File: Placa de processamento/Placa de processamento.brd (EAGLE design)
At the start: 90.2 x 100 mm, 9 parts

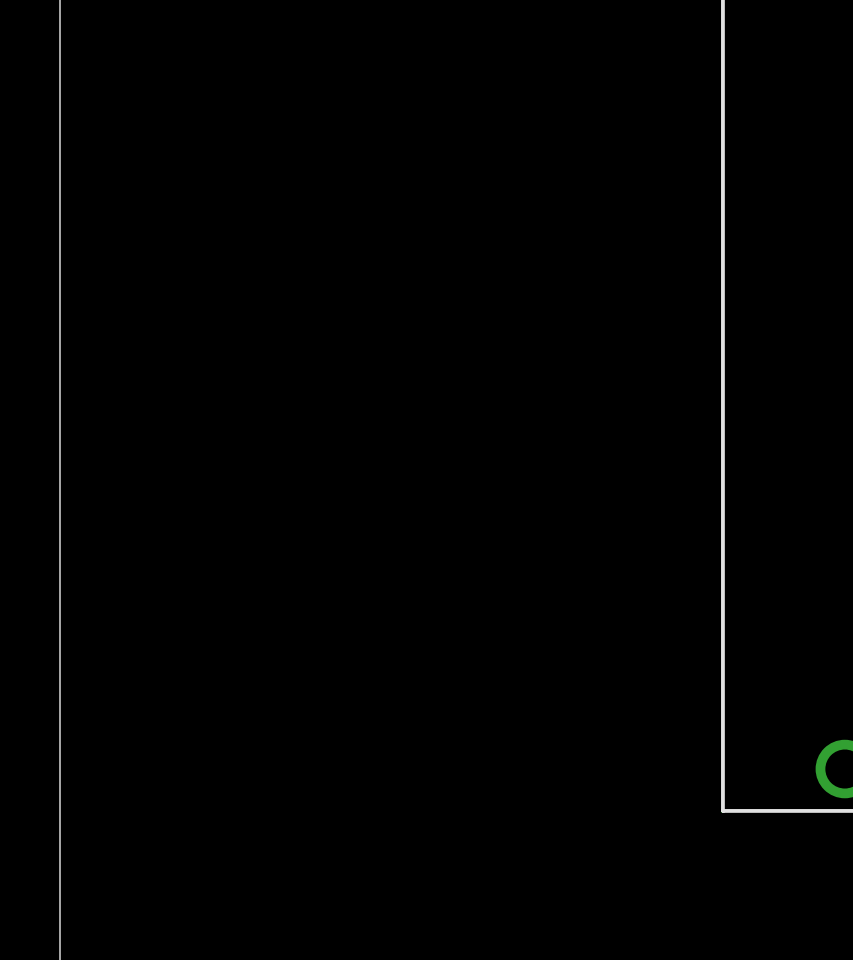
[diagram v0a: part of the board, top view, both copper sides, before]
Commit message: Conexões em placa de processamento
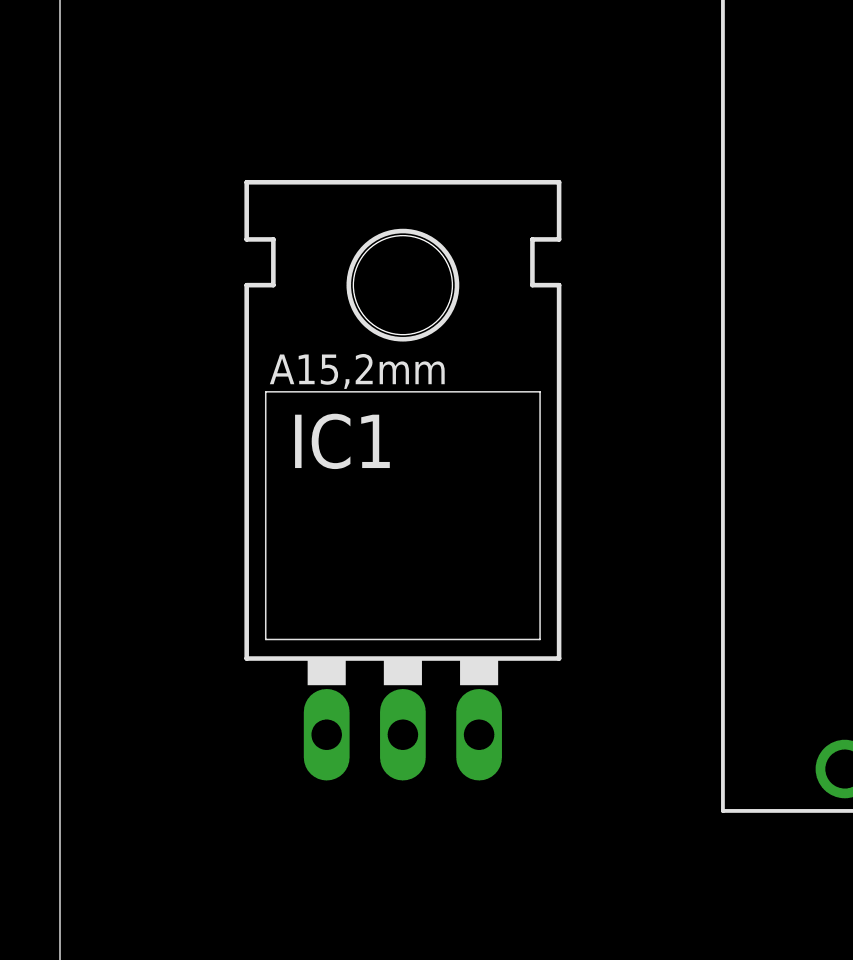
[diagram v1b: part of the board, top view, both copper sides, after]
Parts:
- added IC1: (no value), v-reg:78XXL
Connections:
- new net 3V3: U$2.3V3, U$5.2, U$7.VCC, U$9.1
- new net 5V: IC1.OUT, U$8.VCC
- new net BUZZER: U$5.1, U$9.26
- new net CS: U$2.CS, U$9.8
- new net GND: IC1.GND, U$2.GND, U$3.2, U$7.GND, U$8.GND, U$9.2, U$9.29
- new net M0: U$8.M0, U$9.21
- new net M1: U$8.M1, U$9.22
- new net MISO: U$2.MISO, U$9.10
- new net MOSI: U$2.MOSI, U$9.15
- new net N$3: U$8.AUX
- new net N$5: U$1.PR1
- new net N$6: U$1.PL1
- new net OPTOACOPLADOR1: U$6.1, U$9.19
- new net OPTOACOPLADOR2: U$6.2, U$9.20
- new net RX1: U$7.TX, U$9.3
- new net RX2: U$8.TXD, U$9.6
- new net SCLK: U$2.CLK, U$9.9
- new net SKIB1: U$4.1, U$9.28
- new net SKIB2: U$4.2, U$9.27
- new net TX1: U$7.RX, U$9.5
- new net TX2: U$8.RXD, U$9.7
- new net VIN: IC1.IN, U$1.PL3, U$1.PR3, U$9.30
- new net V_BATTERY: U$1.PL2, U$1.PR2, U$3.1
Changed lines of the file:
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@@
 </layers>
 <board>
-<fusionsync huburn="a.YnVzaW5lc3M6ZGlzY2VudGUxNzg" projecturn="a.YnVzaW5lc3M6ZGlzY2VudGUxNzgjRDIwMjIwNjExNTMyNjQzNTAx" f3durn="urn:adsk.wipprod:dm.lineage:LO0rVtrmTNmc-QnwxbZBTA" pcbguid="9d58484e-0a02-4060-8550-79589bd949fc" lastpulledtime="" lastsyncedchangeguid="" latestrevisionid="46605ec0-6288-40dc-83f6-c90f963cb555" lastsyncedrevisionid="46605ec0-6288-40dc-83f6-c90f963cb555" lastboardhashguid="0044dba3-1b92-d3f1-3d10-6736c9c82925" lastpushedtime="2024-04-18T17:53:33Z" linktopcb3d="true"/>
+<fusionsync huburn="a.YnVzaW5lc3M6ZGlzY2VudGUxNzg" projecturn="a.YnVzaW5lc3M6ZGlzY2VudGUxNzgjRDIwMjIwNjExNTMyNjQzNTAx" f3durn="urn:adsk.wipprod:dm.lineage:LO0rVtrmTNmc-QnwxbZBTA" pcbguid="" lastpulledtime="" lastsyncedchangeguid="" latestrevisionid="46605ec0-6288-40dc-83f6-c90f963cb555" lastsyncedrevisionid="46605ec0-6288-40dc-83f6-c90f963cb555" lastboardhashguid="0044dba3-1b92-d3f1-3d10-6736c9c82925" lastpushedtime="2024-04-18T17:53:33Z" linktopcb3d="true"/>
 <plain>
 <wire x1="0" y1="0" x2="90.15" y2="0" width="0" layer="20"/>
@@
 <attribute name="NAME" x="52.07" y="12.7" size="1.27" layer="21" rot="R90"/>
 </element>
+<element name="IC1" library="v-reg" library_urn="urn:adsk.eagle:library:409" package="78XXL" package3d_urn="urn:adsk.eagle:package:30361/1" value="" x="11.43" y="39.37" smashed="yes">
+<attribute name="NAME" x="7.62" y="44.45" size="1.778" layer="25" ratio="10"/>
+<attribute name="POPULARITY" value="10" x="11.43" y="39.37" size="1.778" layer="27" display="off"/>
+<attribute name="VALUE" x="7.493" y="41.91" size="1.778" layer="27" ratio="10"/>
+</element>
 </elements>
 <signals>
+<signal name="3V3">
+<contactref element="U$9" pad="1"/>
+<contactref element="U$7" pad="VCC"/>
+<contactref element="U$2" pad="3V3"/>
+<contactref element="U$5" pad="2"/>
+<wire x1="17.78" y1="91.44" x2="60.071" y2="78.74" width="0" layer="19" extent="1-1"/>
+<wire x1="79.58" y1="13.96" x2="60.071" y2="78.74" width="0" layer="19" extent="1-1"/>
+<wire x1="6.35" y1="11.63" x2="79.58" y2="13.96" width="0" layer="19" extent="1-1"/>
+</signal>
+<signal name="GND">
+<contactref element="U$9" pad="2"/>
+<contactref element="U$9" pad="29"/>
+<contactref element="U$7" pad="GND"/>
+<contactref element="U$2" pad="GND"/>
+<contactref element="U$8" pad="GND"/>
+<contactref element="U$3" pad="2"/>
+<contactref element="IC1" pad="GND"/>
+<wire x1="41.402" y1="34.417" x2="60.071" y2="66.04" width="0" layer="19" extent="1-1"/>
+<wire x1="54.81" y1="16.5" x2="41.402" y2="34.417" width="0" layer="19" extent="1-1"/>
+<wire x1="79.58" y1="16.5" x2="54.81" y2="16.5" width="0" layer="19" extent="1-1"/>
+<wire x1="6.35" y1="19.25" x2="41.402" y2="34.417" width="0" layer="19" extent="1-1"/>
+<wire x1="11.43" y1="35.56" x2="6.35" y2="19.25" width="0" layer="19" extent="1-1"/>
+<wire x1="7.62" y1="91.44" x2="60.071" y2="66.04" width="0" layer="19" extent="1-1"/>
+</signal>
+<signal name="TX1">
+<contactref element="U$9" pad="5"/>
+<contactref element="U$7" pad="RX"/>
+<wire x1="6.35" y1="14.17" x2="79.58" y2="24.12" width="0" layer="19" extent="1-1"/>
+</signal>
+<signal name="RX1">
+<contactref element="U$9" pad="3"/>
+<contactref element="U$7" pad="TX"/>
+<wire x1="6.35" y1="16.71" x2="79.58" y2="19.04" width="0" layer="19" extent="1-1"/>
+</signal>
+<signal name="MISO">
+<contactref element="U$9" pad="10"/>
+<contactref element="U$2" pad="MISO"/>
+<wire x1="79.58" y1="36.82" x2="60.071" y2="68.58" width="0" layer="19" extent="1-1"/>
+</signal>
+<signal name="MOSI">
+<contactref element="U$9" pad="15"/>
+<contactref element="U$2" pad="MOSI"/>
+<wire x1="79.58" y1="49.52" x2="60.071" y2="73.66" width="0" layer="19" extent="1-1"/>
+</signal>
+<signal name="SCLK">
+<contactref element="U$9" pad="9"/>
+<contactref element="U$2" pad="CLK"/>
+<wire x1="79.58" y1="34.28" x2="60.071" y2="71.12" width="0" layer="19" extent="1-1"/>
+</signal>
+<signal name="CS">
+<contactref element="U$9" pad="8"/>
+<contactref element="U$2" pad="CS"/>
+<wire x1="79.58" y1="31.74" x2="60.071" y2="76.2" width="0" layer="19" extent="1-1"/>
+</signal>
+<signal name="M0">
+<contactref element="U$9" pad="21"/>
+<contactref element="U$8" pad="M0"/>
+<wire x1="26.162" y1="34.417" x2="54.81" y2="36.82" width="0" layer="19" extent="1-1"/>
+</signal>
+<signal name="M1">
+<contactref element="U$9" pad="22"/>
+<contactref element="U$8" pad="M1"/>
+<wire x1="28.702" y1="34.417" x2="54.81" y2="34.28" width="0" layer="19" extent="1-1"/>
+</signal>
+<signal name="RX2">
+<contactref element="U$9" pad="6"/>
+<contactref element="U$8" pad="TXD"/>
+<wire x1="33.782" y1="34.417" x2="79.58" y2="26.66" width="0" layer="19" extent="1-1"/>
+</signal>
+<signal name="TX2">
+<contactref element="U$9" pad="7"/>
+<contactref element="U$8" pad="RXD"/>
+<wire x1="31.242" y1="34.417" x2="79.58" y2="29.2" width="0" layer="19" extent="1-1"/>
+</signal>
+<signal name="N$3">
+<contactref element="U$8" pad="AUX"/>
+</signal>
+<signal name="V_BATTERY">
+<contactref element="U$3" pad="1"/>
+<contactref element="U$1" pad="PR2"/>
+<contactref element="U$1" pad="PL2"/>
+<wire x1="67.587" y1="90.138" x2="67.587" y2="92.638" width="0" layer="19" extent="1-1"/>
+<wire x1="5.08" y1="91.44" x2="67.587" y2="92.638" width="0" layer="19" extent="1-1"/>
+</signal>
+<signal name="VIN">
+<contactref element="U$1" pad="PR3"/>
+<contactref element="U$1" pad="PL3"/>
+<contactref element="U$9" pad="30"/>
+<contactref element="IC1" pad="IN"/>
+<wire x1="70.587" y1="90.138" x2="70.587" y2="92.638" width="0" layer="19" extent="1-1"/>
+<wire x1="54.81" y1="13.96" x2="70.587" y2="90.138" width="0" layer="19" extent="1-1"/>
+<wire x1="8.89" y1="35.56" x2="54.81" y2="13.96" width="0" layer="19" extent="1-1"/>
+</signal>
+<signal name="N$5">
+<contactref element="U$1" pad="PR1"/>
+</signal>
+<signal name="N$6">
+<contactref element="U$1" pad="PL1"/>
+</signal>
+<signal name="5V">
+<contactref element="IC1" pad="OUT"/>
+<contactref element="U$8" pad="VCC"/>
+<wire x1="13.97" y1="35.56" x2="38.862" y2="34.417" width="0" layer="19" extent="1-1"/>
+</signal>
+<signal name="SKIB1">
+<contactref element="U$4" pad="1"/>
+<contactref element="U$9" pad="28"/>
+<wire x1="54.81" y1="19.04" x2="15.24" y2="82.55" width="0" layer="19" extent="1-1"/>
+</signal>
+<signal name="SKIB2">
+<contactref element="U$4" pad="2"/>
+<contactref element="U$9" pad="27"/>
+<wire x1="54.81" y1="21.58" x2="17.78" y2="82.55" width="0" layer="19" extent="1-1"/>
+</signal>
+<signal name="BUZZER">
+<contactref element="U$5" pad="1"/>
+<contactref element="U$9" pad="26"/>
+<wire x1="54.81" y1="24.12" x2="15.24" y2="91.44" width="0" layer="19" extent="1-1"/>
+</signal>
+<signal name="OPTOACOPLADOR1">
+<contactref element="U$6" pad="1"/>
+<contactref element="U$9" pad="19"/>
+<wire x1="5.08" y1="82.55" x2="54.81" y2="41.9" width="0" layer="19" extent="1-1"/>
+</signal>
+<signal name="OPTOACOPLADOR2">
+<contactref element="U$6" pad="2"/>
+<contactref element="U$9" pad="20"/>
+<wire x1="7.62" y1="82.55" x2="54.81" y2="39.36" width="0" layer="19" extent="1-1"/>
+</signal>
 </signals>
 <mfgpreviewcolors>

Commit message: Começo do roteamento
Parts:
- moved U$7 2.54 mm to (25.4, 15.2)
- moved U$3 2.54 mm to (6.35, 88.9)
- moved U$4 2.54 mm to (16.5, 80.0)
- moved U$5 2.54 mm to (16.5, 88.9)
- moved U$6 2.54 mm to (6.35, 80.0)
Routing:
- net VIN: track 0.00 -> 262.1 mm
- net 3V3: track 0.00 -> 210.3 mm
- net RX2: track 0.00 -> 142.1 mm, vias 0 -> 2
- net TX2: track 0.00 -> 122.5 mm
- net BUZZER: track 0.00 -> 102.1 mm, vias 0 -> 2
- net TX1: track 0.00 -> 93.6 mm
- net RX1: track 0.00 -> 79.4 mm
- net SKIB1: track 0.00 -> 79.2 mm, vias 0 -> 2
- net V_BATTERY: track 0.00 -> 76.5 mm
- net SKIB2: track 0.00 -> 75.2 mm, vias 0 -> 2
- net OPTOACOPLADOR1: track 0.00 -> 69.5 mm, vias 0 -> 2
- net OPTOACOPLADOR2: track 0.00 -> 67.4 mm, vias 0 -> 2
- net CS: track 0.00 -> 60.4 mm
- net SCLK: track 0.00 -> 49.7 mm
- net 5V: track 0.00 -> 46.4 mm
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- added copper zone on layer 16, net GND

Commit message: Update do roteamento
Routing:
- net TX1: track 93.6 -> 94.8 mm
- net OPTOACOPLADOR1: track 69.5 -> 70.3 mm
- net RX2: track 142.1 -> 142.8 mm
- net OPTOACOPLADOR2: track 67.4 -> 68.1 mm
- net GND: track 0.51 -> 0.00 mm, vias 0 -> 1
- added copper zone on layer 1, net GND

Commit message: Placas
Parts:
- added U$10: JST2.54X2P, CRD:JST2.54X2P_FOOTPRINT
- moved U$4 1.27 mm to (15.2, 80.0)
- moved U$5 1.27 mm to (15.2, 88.9)
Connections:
- removed net N$5: U$1.PR1
- removed net N$6: U$1.PL1
- new net RX0: U$10.1, U$9.12
- new net TX0: U$10.2, U$9.13
- net VIN: now also U$1.PL2, U$1.PR2; no longer U$1.PL3, U$1.PR3
- net V_BATTERY: now also U$1.PL1, U$1.PR1; no longer U$1.PL2, U$1.PR2
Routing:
- net RX0: track 0.00 -> 87.1 mm, vias 0 -> 2
- net TX0: track 0.00 -> 82.3 mm, vias 0 -> 2
- net V_BATTERY: track 76.5 -> 95.5 mm
- net 3V3: track 210.3 -> 227.0 mm
- net RX2: track 142.8 -> 139.0 mm
- net SKIB1: track 79.2 -> 82.7 mm
- net SKIB2: track 75.2 -> 78.7 mm
- net OPTOACOPLADOR2: track 68.1 -> 71.1 mm
- net SCLK: track 50.0 -> 52.2 mm
- net BUZZER: track 102.1 -> 100.3 mm
- net VIN: track 262.1 -> 263.3 mm
- net MISO: track 43.7 -> 44.7 mm
- net TX2: track 122.5 -> 121.8 mm

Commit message: Atualização
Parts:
- added SP1: AL11P, buzzer:AL11P
- moved IC1 1.27 mm to (10.2, 39.4)
- moved U$7 0.52 mm to (25.3, 15.7), flipped to the bottom, turned to 90 degrees
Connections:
- new net SIGNAL1: U$5.1, U$9.26
- net BUZZER: now also SP1.+, U$9.24; no longer U$5.1, U$9.26
- net GND: now also SP1.-
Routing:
- net SIGNAL1: track 0.00 -> 96.7 mm, vias 0 -> 2
- net BUZZER: track 100.3 -> 57.4 mm
- net TX1: track 94.8 -> 79.1 mm
- net 3V3: track 227.0 -> 242.1 mm
- net M1: track 32.1 -> 35.3 mm
- net M0: track 36.5 -> 39.6 mm
- net RX1: track 79.3 -> 78.4 mm
- net 5V: track 46.4 -> 46.9 mm
